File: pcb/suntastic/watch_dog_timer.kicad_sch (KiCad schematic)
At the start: 4 parts, among them SW1 SW_Push, U7 TPL5010

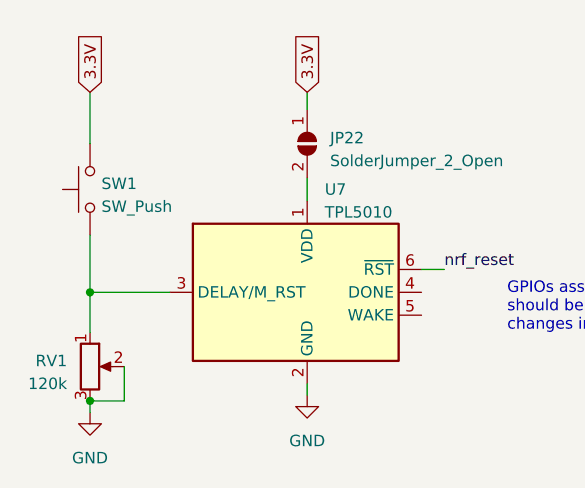
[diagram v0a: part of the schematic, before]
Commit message: Update footprints
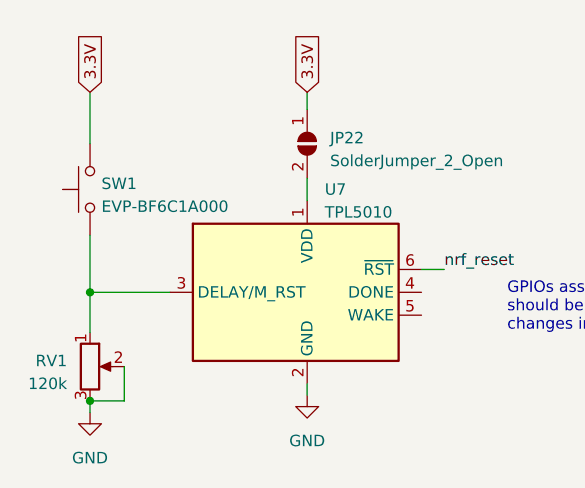
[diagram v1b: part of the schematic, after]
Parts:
- JP22: footprint (none) -> Jumper:SolderJumper-2_P1.3mm_Open_RoundedPad1.0x1.5mm
- SW1: value SW_Push -> EVP-BF6C1A000; footprint (none) -> Button_Switch_SMD:SW_SPST_EVPBF
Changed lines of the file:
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@@
       (effects (font (size 1.27 1.27)) (justify left))
     )
-    (property "Footprint" "" (at 137.16 58.42 0)
+    (property "Footprint" "Jumper:SolderJumper-2_P1.3mm_Open_RoundedPad1.0x1.5mm" (at 137.16 58.42 0)
       (effects (font (size 1.27 1.27)) hide)
     )
@@
       (effects (font (size 1.27 1.27)) (justify right))
     )
-    (property "Value" "SW_Push" (at 114.3 65.405 90)
+    (property "Value" "EVP-BF6C1A000" (at 114.3 65.405 90)
       (effects (font (size 1.27 1.27)) (justify right))
     )
-    (property "Footprint" "" (at 107.95 63.5 0)
+    (property "Footprint" "Button_Switch_SMD:SW_SPST_EVPBF" (at 107.95 63.5 0)
       (effects (font (size 1.27 1.27)) hide)
     )
-    (property "Datasheet" "~" (at 107.95 63.5 0)
+    (property "Datasheet" "https://mm.digikey.com/Volume0/opasdata/d220001/medias/docus/308/EVP-BF_Series_DS.pdf" (at 107.95 63.5 0)
       (effects (font (size 1.27 1.27)) hide)
     )

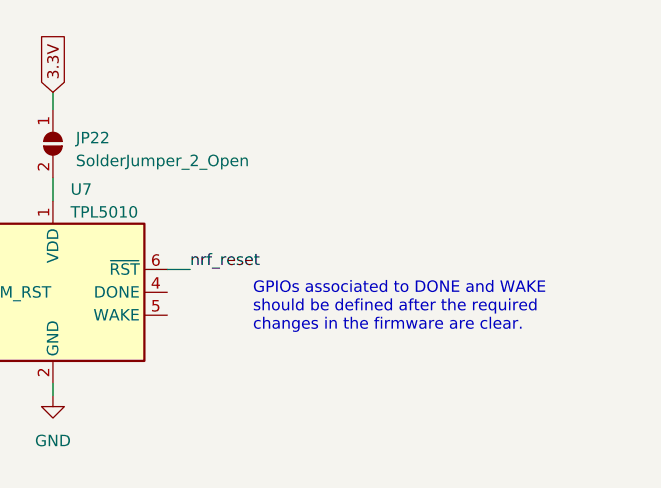
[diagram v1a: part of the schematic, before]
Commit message: Update more footprints and start with PCB
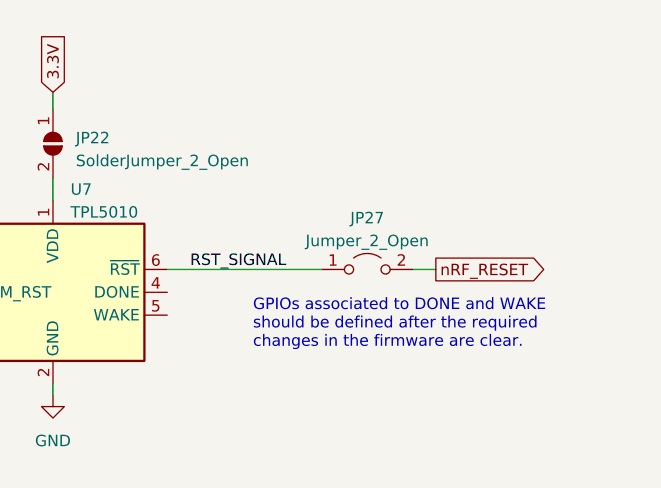
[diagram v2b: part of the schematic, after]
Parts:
- added JP27: Jumper_2_Open, Jumper:SolderJumper-2_P1.3mm_Open_RoundedPad1.0x1.5mm, symbol Jumper:Jumper_2_Open
- RV1: footprint (none) -> Potentiometer_THT:Potentiometer_Bourns_3296W_Vertical
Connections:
- net nrf_reset renamed RST_SIGNAL
- net RST_SIGNAL: now also JP27.1 (A)
- new net nRF_RESET: JP27.2 (B)
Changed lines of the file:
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@@
     (stroke (width 0) (type default))
   )
-  (wire (pts (xy 149.86 72.39) (xy 152.4 72.39))
+  (wire (pts (xy 177.165 72.39) (xy 179.705 72.39))
     (stroke (width 0) (type default))
   )
@@
   )
   (wire (pts (xy 113.03 79.375) (xy 113.03 74.93))
+    (stroke (width 0) (type default))
+  )
+  (wire (pts (xy 149.86 72.39) (xy 167.005 72.39))
     (stroke (width 0) (type default))
   )
@@
   )
   (text "GPIOs associated to DONE and WAKE\nshould be defined after the required\nchanges in the firmware are clear."
-    (at 159.385 79.375 0)
+    (at 159.385 81.28 0)
     (effects (font (size 1.27 1.27)) (justify left bottom))
   )
-  (label "nrf_reset" (at 152.4 72.39 0) (fields_autoplaced)
+  (label "RST_SIGNAL" (at 152.4 72.39 0) (fields_autoplaced)
     (effects (font (size 1.27 1.27)) (justify left bottom))
   )
@@
     (effects (font (size 1.27 1.27)) (justify left))
     (property "Intersheetrefs" "${INTERSHEET_REFS}" (at 137.16 45.6868 90)
+      (effects (font (size 1.27 1.27)) (justify left) hide)
+    )
+  )
+  (global_label "nRF_RESET" (shape output) (at 179.705 72.39 0) (fields_autoplaced)
+    (effects (font (size 1.27 1.27)) (justify left))
+    (property "Intersheetrefs" "${INTERSHEET_REFS}" (at 192.8311 72.39 0)
       (effects (font (size 1.27 1.27)) (justify left) hide)
     )
@@
     )
   )
+  (symbol (lib_id "Jumper:Jumper_2_Open") (at 172.085 72.39 0) (unit 1)
+    (in_bom yes) (on_board yes) (dnp no) (fields_autoplaced)
+    (property "Reference" "JP27" (at 172.085 66.675 0)
+      (effects (font (size 1.27 1.27)))
+    )
+    (property "Value" "Jumper_2_Open" (at 172.085 69.215 0)
+      (effects (font (size 1.27 1.27)))
+    )
+    (property "Footprint" "Jumper:SolderJumper-2_P1.3mm_Open_RoundedPad1.0x1.5mm" (at 172.085 72.39 0)
+      (effects (font (size 1.27 1.27)) hide)
+    )
+    (property "Datasheet" "~" (at 172.085 72.39 0)
+      (effects (font (size 1.27 1.27)) hide)
+    )
+    (pin "1")
+    (pin "2")
+    (instances
+      (project "suntastic"
+        (path "/4d5a6178-89d6-4824-ac30-5dee40aabff2/a38aadbc-1307-4a96-a364-cee9c7cfea8a"
+          (reference "JP27") (unit 1)
+        )
+      )
+    )
+  )
   (symbol (lib_id "Device:R_Potentiometer") (at 113.03 83.185 0) (unit 1)
     (in_bom yes) (on_board yes) (dnp no) (fields_autoplaced)
@@
       (effects (font (size 1.27 1.27)) (justify right))
     )
-    (property "Footprint" "" (at 113.03 83.185 0)
+    (property "Footprint" "Potentiometer_THT:Potentiometer_Bourns_3296W_Vertical" (at 113.03 83.185 0)
       (effects (font (size 1.27 1.27)) hide)
     )

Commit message: Rework watchdog
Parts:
- removed JP27: Jumper_2_Open, Jumper:SolderJumper-2_P1.3mm_Open_RoundedPad1.0x1.5mm, symbol Jumper:Jumper_2_Open
- added C23: 1uF, Capacitor_SMD:C_0603_1608Metric_Pad1.08x0.95mm_HandSolder, symbol Device:C
- added JP28: SolderJumper_2_Open, Jumper:SolderJumper-2_P1.3mm_Open_RoundedPad1.0x1.5mm, symbol Jumper:SolderJumper_2_Open
- added R4, R7, R8: R, Resistor_SMD:R_0603_1608Metric_Pad0.98x0.95mm_HandSolder, symbol Device:R
- added U9: TPS22917DBV, Package_TO_SOT_SMD:SOT-23-6, symbol Power_Management:TPS22917DBV
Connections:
- net GND: now also C23.2, R7.2, U9.2 (GND)
- net RST_SIGNAL: now also R8.2
- net at U7.4 (DONE): now also C23.1, JP28.1 (A), U9.6 (VOUT)
- net at U7.5 (WAKE): now also R4.1
- net 3.3V renamed V_boost_uvlo
- net V_boost_uvlo: now also R8.1, U9.1 (VIN)
- new net: JP28.2 (B), U9.5 (QOD)
- new net GPIO_DONE: U9.3 (ON)
- new net GPIO_WAKE: R4.2, R7.1
- no-connect marks 0 -> 1
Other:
- note added: "This load switch is acting as a level shifter."

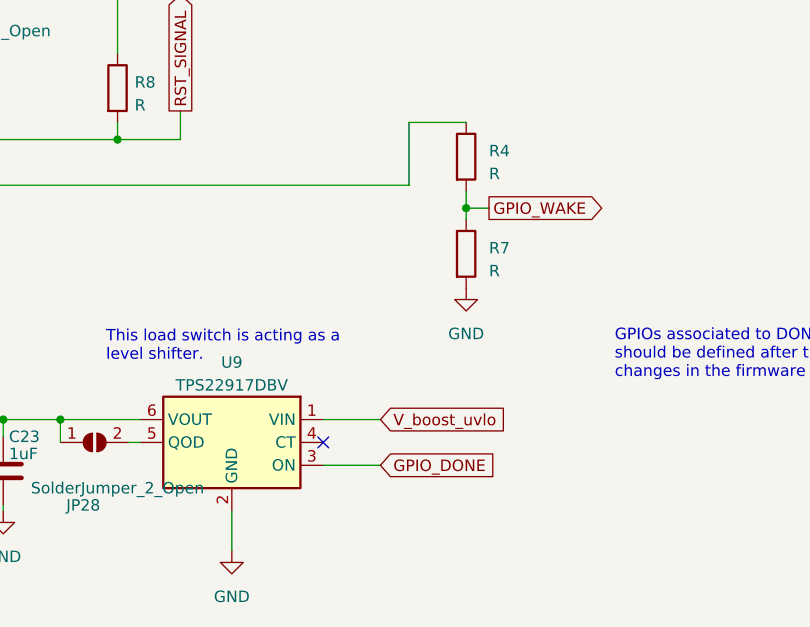
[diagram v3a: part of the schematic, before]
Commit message: Add screw terminals for external MPPT module and PV input
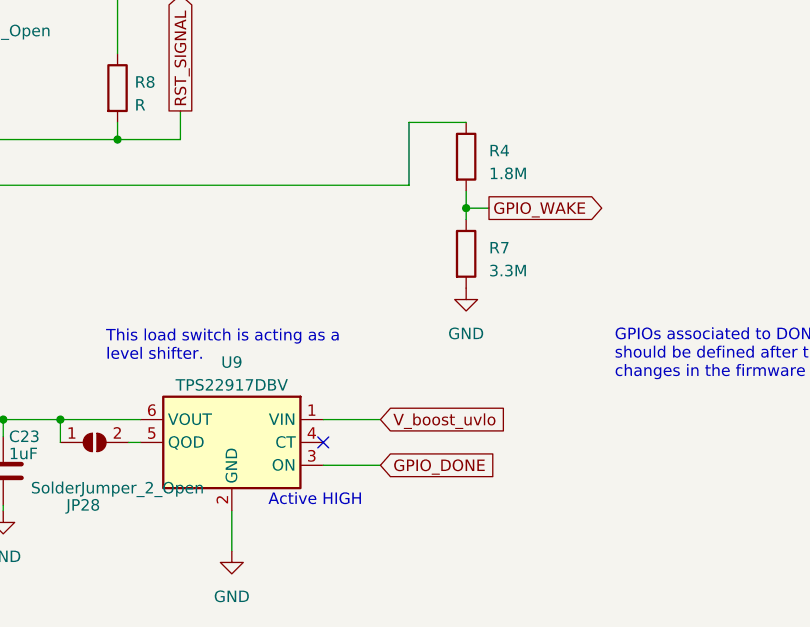
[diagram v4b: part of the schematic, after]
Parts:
- R4: value R -> 1.8M
- R7: value R -> 3.3M
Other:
- note added: "Active HIGH"
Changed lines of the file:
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@@
+    (effects (font (size 1.27 1.27)) (justify left bottom))
+  )
+  (text "Active HIGH" (at 183.134 113.284 0)
     (effects (font (size 1.27 1.27)) (justify left bottom))
   )
@@
       (effects (font (size 1.27 1.27)) (justify left))
     )
-    (property "Value" "R" (at 207.645 86.995 0)
+    (property "Value" "3.3M" (at 207.645 86.995 0)
       (effects (font (size 1.27 1.27)) (justify left))
     )
@@
       (effects (font (size 1.27 1.27)) (justify left))
     )
-    (property "Value" "R" (at 207.645 76.2 0)
-      (effects (font (size 1.27 1.27)) (justify left))
-    )
+    (property "Value" "1.8M" (at 207.645 76.2 0)
+      (effects (font (size 1.27 1.27)) (justify left))
+    )
